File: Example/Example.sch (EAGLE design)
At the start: 27 parts, among them IC2 74LS02D, U1 CD4017

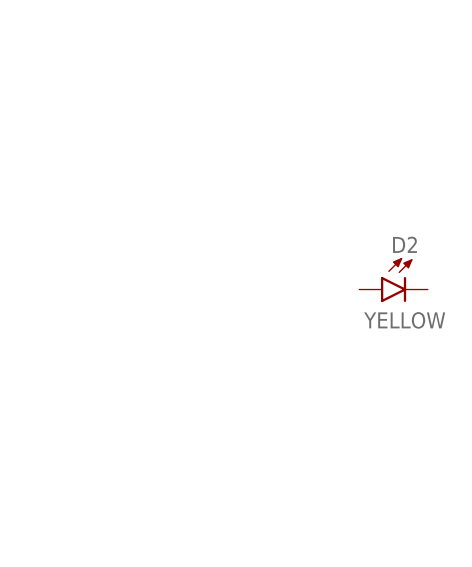
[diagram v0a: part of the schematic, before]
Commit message: placed items on board
i placed everything on the board except for battery holders
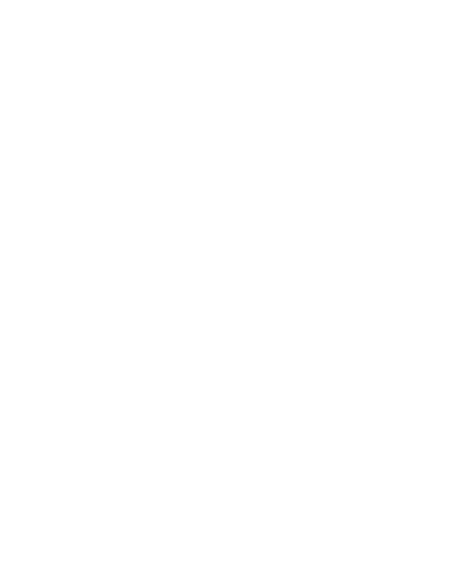
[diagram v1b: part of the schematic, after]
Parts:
- removed D2: YELLOW, RoboJackets-LEDs:LED-SMD-YELLOW
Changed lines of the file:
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@@
 <part name="S1" library="adafruit" library_urn="urn:adsk.eagle:library:420" deviceset="40-XX" device="-ROUND" package3d_urn="urn:adsk.eagle:package:6240926/1"/>
 <part name="U$1" library="adafruit" library_urn="urn:adsk.eagle:library:420" deviceset="CR1220" device="SMT" package3d_urn="urn:adsk.eagle:package:6240665/1"/>
-<part name="D2" library="RoboJackets-LEDs" deviceset="LED-SMD" device="" technology="-YELLOW" value="YELLOW"/>
 <part name="D3" library="RoboJackets-LEDs" deviceset="LED-SMD" device="" technology="-YELLOW" value="YELLOW"/>
 <part name="R1" library="rcl" library_urn="urn:adsk.eagle:library:334" deviceset="R-US_" device="R0603" package3d_urn="urn:adsk.eagle:package:23555/3"/>
@@
 <attribute name="VALUE" x="29.21" y="99.06" size="1.778" layer="96"/>
 </instance>
-<instance part="D2" gate="A" x="243.84" y="119.38" smashed="yes">
-<attribute name="NAME" x="243.84" y="123.444" size="1.778" layer="95" rot="MR0" align="bottom-center"/>
-<attribute name="VALUE" x="243.84" y="116.84" size="1.778" layer="96" rot="MR0" align="top-center"/>
-</instance>
 <instance part="D3" gate="A" x="162.56" y="99.06" smashed="yes">

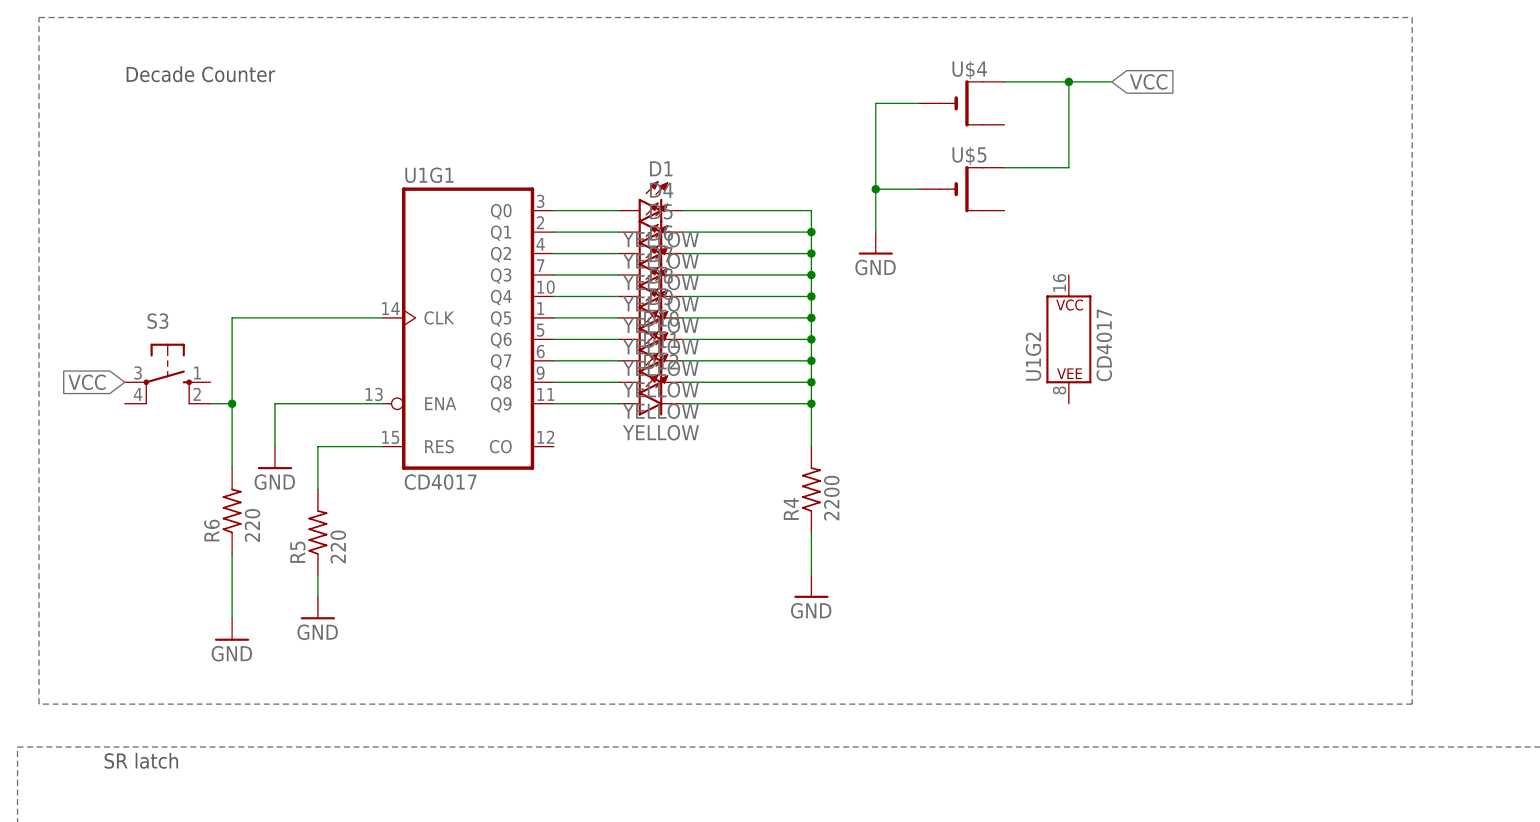
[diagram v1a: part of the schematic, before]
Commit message: Added LEDs, made one Vcc, and updated board
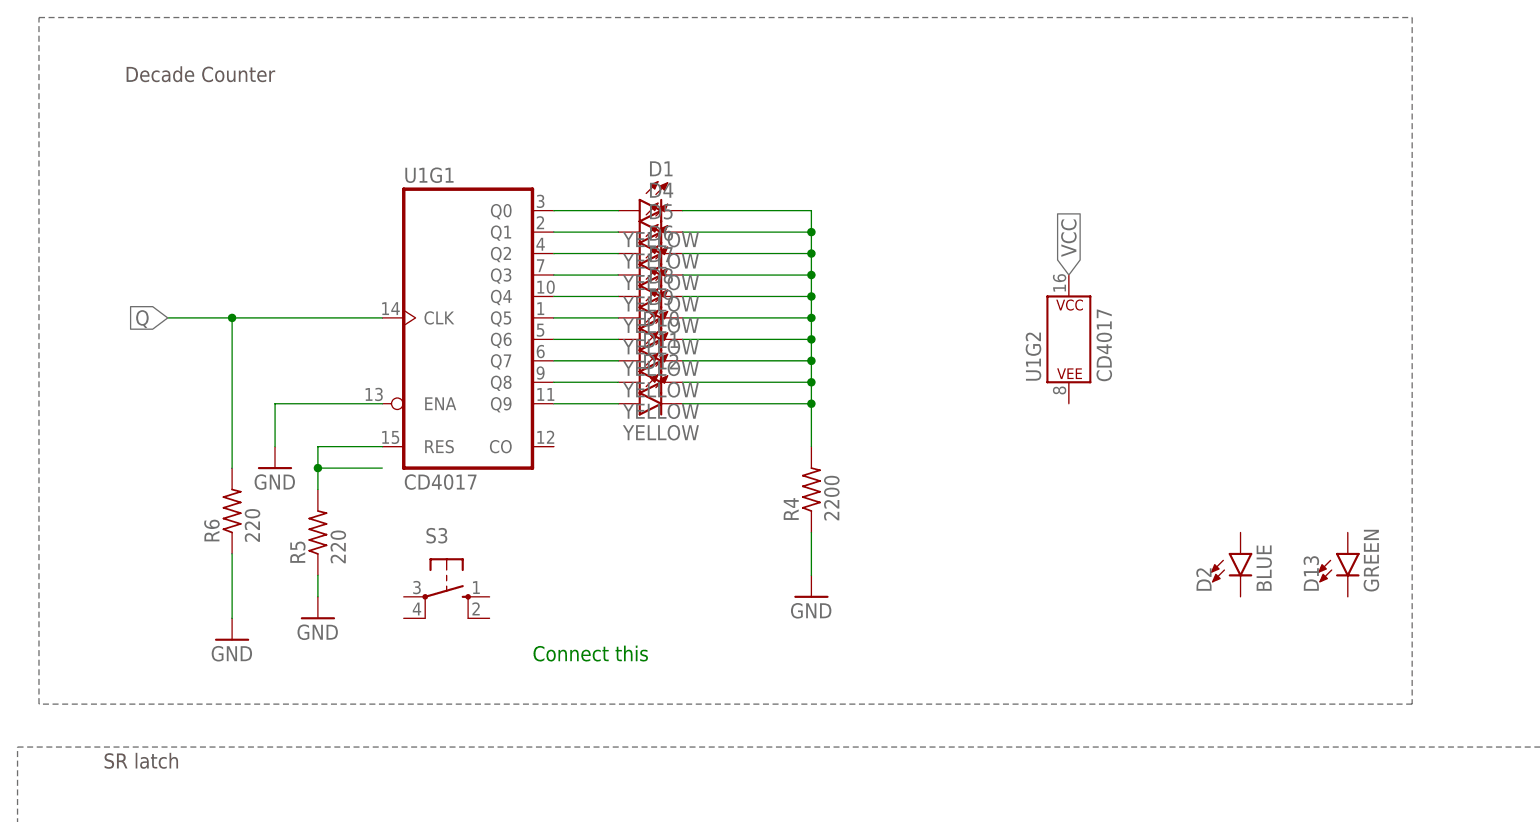
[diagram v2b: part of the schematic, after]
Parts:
- removed U$4, U$5: (no value), adafruit:CR1220SMT
- added D13: GREEN, RoboJackets-LEDs:LED-GREEN0603
- added D2: BLUE, RoboJackets-LEDs:LED-BLUE0603
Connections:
- removed net N$1: R6.2, S3.S1, U1G1.CLK
- net GND: no longer U$4.-, U$5.-
- net Q: now also R6.2, U1G1.CLK
- net VCC: no longer U$4.+, U$5.+
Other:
- note added: "Connect this"
- moved on the sheet: S3
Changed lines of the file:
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@@
 <part name="R6" library="rcl" library_urn="urn:adsk.eagle:library:334" deviceset="R-US_" device="R0603" package3d_urn="urn:adsk.eagle:package:23555/3" value="220"/>
 <part name="SUPPLY1" library="RoboJackets-Supplies" deviceset="GND" device=""/>
-<part name="U$4" library="adafruit" library_urn="urn:adsk.eagle:library:420" deviceset="CR1220" device="SMT" package3d_urn="urn:adsk.eagle:package:6240665/1"/>
-<part name="U$5" library="adafruit" library_urn="urn:adsk.eagle:library:420" deviceset="CR1220" device="SMT" package3d_urn="urn:adsk.eagle:package:6240665/1"/>
-<part name="SUPPLY2" library="RoboJackets-Supplies" deviceset="GND" device=""/>
 <part name="SUPPLY3" library="RoboJackets-Supplies" deviceset="GND" device=""/>
+<part name="D2" library="RoboJackets-LEDs" deviceset="LED-BLUE" device="0603" value="BLUE"/>
+<part name="D13" library="RoboJackets-LEDs" deviceset="LED-GREEN" device="0603" value="GREEN"/>
 </parts>
 <sheets>
 <sheet>
-<description>555 Timer Motor Driver Circuit</description>
+<description>Decade Counter with SR Latch Game</description>
 <plain>
 <text x="17.78" y="119.38" size="1.778" layer="97">SR latch</text>
@@
 <wire x1="154.94" y1="2.54" x2="7.62" y2="2.54" width="0.1524" layer="95" style="shortdash"/>
 <wire x1="7.62" y1="2.54" x2="7.62" y2="121.92" width="0.1524" layer="95" style="shortdash"/>
+<text x="68.58" y="132.08" size="1.778" layer="91">Connect this</text>
 </plain>
 <instances>
@@
 <attribute name="VALUE" x="40.64" y="134.62" size="1.778" layer="96"/>
 </instance>
-<instance part="S3" gate="1" x="25.4" y="165.1" smashed="yes" rot="R270">
-<attribute name="NAME" x="22.86" y="171.45" size="1.778" layer="95"/>
-<attribute name="VALUE" x="28.575" y="168.91" size="1.778" layer="96"/>
+<instance part="S3" gate="1" x="58.42" y="139.7" smashed="yes" rot="R270">
+<attribute name="NAME" x="55.88" y="146.05" size="1.778" layer="95"/>
+<attribute name="VALUE" x="61.595" y="143.51" size="1.778" layer="96"/>
 </instance>
 <instance part="R6" gate="G$1" x="33.02" y="149.86" smashed="yes" rot="R90">
@@
 <attribute name="VALUE" x="30.48" y="132.08" size="1.778" layer="96"/>
 </instance>
-<instance part="U$4" gate="G$1" x="119.38" y="198.12" smashed="yes">
-<attribute name="NAME" x="118.11" y="201.295" size="1.778" layer="95"/>
-<attribute name="VALUE" x="118.11" y="193.04" size="1.778" layer="96"/>
-</instance>
-<instance part="U$5" gate="G$1" x="119.38" y="187.96" smashed="yes">
-<attribute name="NAME" x="118.11" y="191.135" size="1.778" layer="95"/>
-<attribute name="VALUE" x="118.11" y="182.88" size="1.778" layer="96"/>
-</instance>
-<instance part="SUPPLY2" gate="G$1" x="109.22" y="180.34" smashed="yes">
-<attribute name="VALUE" x="106.68" y="177.8" size="1.778" layer="96"/>
-</instance>
 <instance part="SUPPLY3" gate="G$1" x="38.1" y="154.94" smashed="yes">
 <attribute name="VALUE" x="35.56" y="152.4" size="1.778" layer="96"/>
+</instance>
+<instance part="D2" gate="G$1" x="152.4" y="144.78" smashed="yes">
+<attribute name="NAME" x="148.971" y="140.208" size="1.778" layer="95" font="vector" rot="R90"/>
+<attribute name="VALUE" x="154.305" y="140.208" size="1.778" layer="96" font="vector" rot="R90" align="top-left"/>
+</instance>
+<instance part="D13" gate="G$1" x="165.1" y="144.78" smashed="yes">
+<attribute name="NAME" x="161.671" y="140.208" size="1.778" layer="95" font="vector" rot="R90"/>
+<attribute name="VALUE" x="167.005" y="140.208" size="1.778" layer="96" font="vector" rot="R90" align="top-left"/>
 </instance>
 </instances>
@@
 </segment>
 <segment>
-<pinref part="U$4" gate="G$1" pin="-"/>
-<wire x1="114.3" y1="198.12" x2="109.22" y2="198.12" width="0.1524" layer="91"/>
-<wire x1="109.22" y1="198.12" x2="109.22" y2="187.96" width="0.1524" layer="91"/>
-<pinref part="U$5" gate="G$1" pin="-"/>
-<wire x1="109.22" y1="187.96" x2="109.22" y2="182.88" width="0.1524" layer="91"/>
-<wire x1="114.3" y1="187.96" x2="109.22" y2="187.96" width="0.1524" layer="91"/>
-<junction x="109.22" y="187.96"/>
-<pinref part="SUPPLY2" gate="G$1" pin="GND"/>
-</segment>
-<segment>
 <pinref part="U1" gate="G1" pin="ENA"/>
 <wire x1="50.8" y1="162.56" x2="38.1" y2="162.56" width="0.1524" layer="91"/>
@@
 <segment>
 <label x="152.4" y="99.06" size="1.778" layer="95" rot="R180" xref="yes"/>
+</segment>
+<segment>
+<pinref part="R6" gate="G$1" pin="2"/>
+<wire x1="33.02" y1="154.94" x2="33.02" y2="172.72" width="0.1524" layer="91"/>
+<pinref part="U1" gate="G1" pin="CLK"/>
+<wire x1="50.8" y1="172.72" x2="33.02" y2="172.72" width="0.1524" layer="91"/>
+<wire x1="33.02" y1="172.72" x2="25.4" y2="172.72" width="0.1524" layer="91"/>
+<junction x="33.02" y="172.72"/>
+<label x="25.4" y="172.72" size="1.778" layer="95" rot="R180" xref="yes"/>
 </segment>
 </net>
@@
 </segment>
 <segment>
-<pinref part="U$4" gate="G$1" pin="+"/>
-<wire x1="124.46" y1="200.66" x2="132.08" y2="200.66" width="0.1524" layer="91"/>
-<pinref part="U$5" gate="G$1" pin="+"/>
-<wire x1="132.08" y1="200.66" x2="137.16" y2="200.66" width="0.1524" layer="91"/>
-<wire x1="124.46" y1="190.5" x2="132.08" y2="190.5" width="0.1524" layer="91"/>
-<wire x1="132.08" y1="190.5" x2="132.08" y2="200.66" width="0.1524" layer="91"/>
-<junction x="132.08" y="200.66"/>
-<label x="137.16" y="200.66" size="1.778" layer="95" xref="yes"/>
-</segment>
-<segment>
-<label x="20.32" y="165.1" size="1.778" layer="95" rot="R180" xref="yes"/>
+<label x="132.08" y="177.8" size="1.778" layer="95" rot="R90" xref="yes"/>
 </segment>
 </net>
@@
 <pinref part="U1" gate="G1" pin="RES"/>
 <wire x1="50.8" y1="157.48" x2="43.18" y2="157.48" width="0.1524" layer="91"/>
-<wire x1="43.18" y1="157.48" x2="43.18" y2="152.4" width="0.1524" layer="91"/>
+<wire x1="43.18" y1="157.48" x2="43.18" y2="154.94" width="0.1524" layer="91"/>
 <pinref part="R5" gate="G$1" pin="2"/>
-</segment>
-</net>
-<net name="N$1" class="0">
-<segment>
-<pinref part="S3" gate="1" pin="S1"/>
-<wire x1="30.48" y1="162.56" x2="33.02" y2="162.56" width="0.1524" layer="91"/>
-<pinref part="R6" gate="G$1" pin="2"/>
-<wire x1="33.02" y1="154.94" x2="33.02" y2="162.56" width="0.1524" layer="91"/>
-<wire x1="33.02" y1="162.56" x2="33.02" y2="172.72" width="0.1524" layer="91"/>
-<junction x="33.02" y="162.56"/>
-<pinref part="U1" gate="G1" pin="CLK"/>
-<wire x1="50.8" y1="172.72" x2="33.02" y2="172.72" width="0.1524" layer="91"/>
-</segment>
-</net>
+<wire x1="43.18" y1="154.94" x2="43.18" y2="152.4" width="0.1524" layer="91"/>
+<wire x1="50.8" y1="154.94" x2="43.18" y2="154.94" width="0.1524" layer="91"/>
+<junction x="43.18" y="154.94"/>
+</segment>
+</net>
